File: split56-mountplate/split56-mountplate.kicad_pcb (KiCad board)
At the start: 2 copper layers, 139.2 x 82 mm, 12 parts

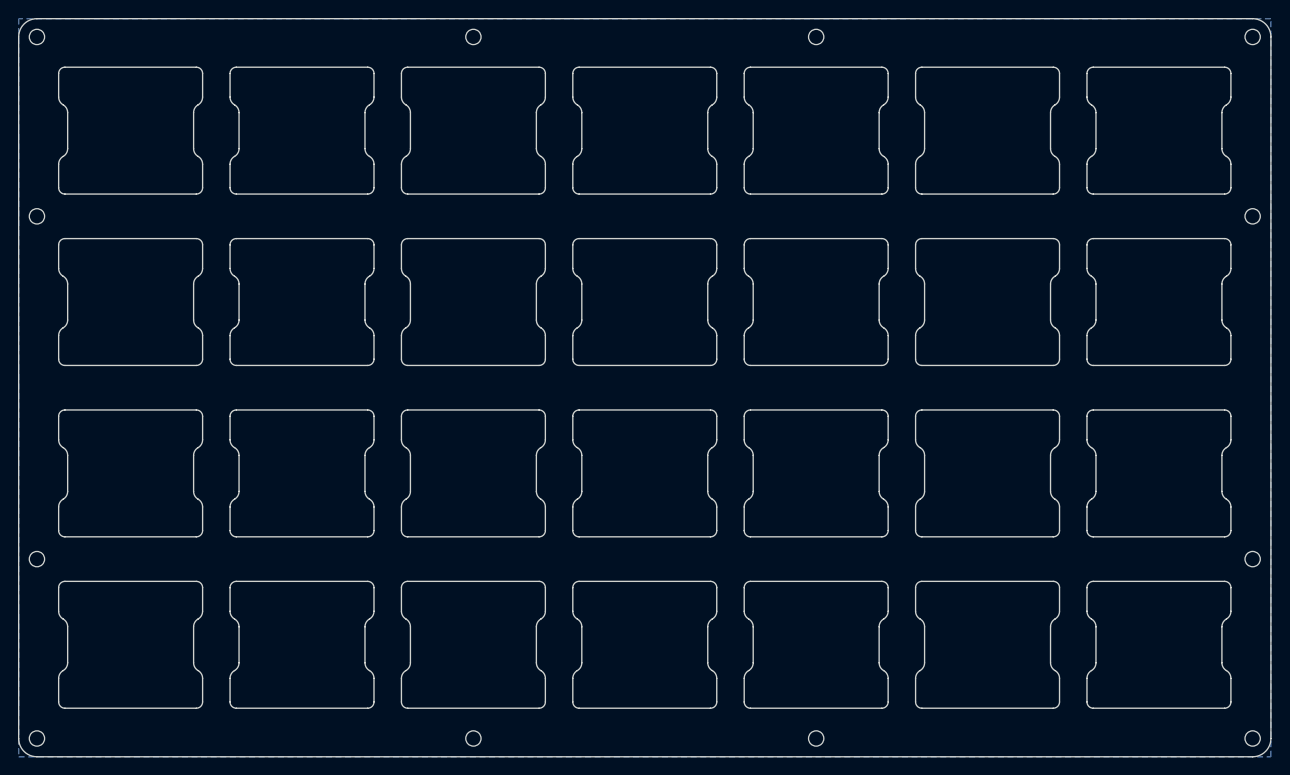
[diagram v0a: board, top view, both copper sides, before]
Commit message: Fix mount plate hole size
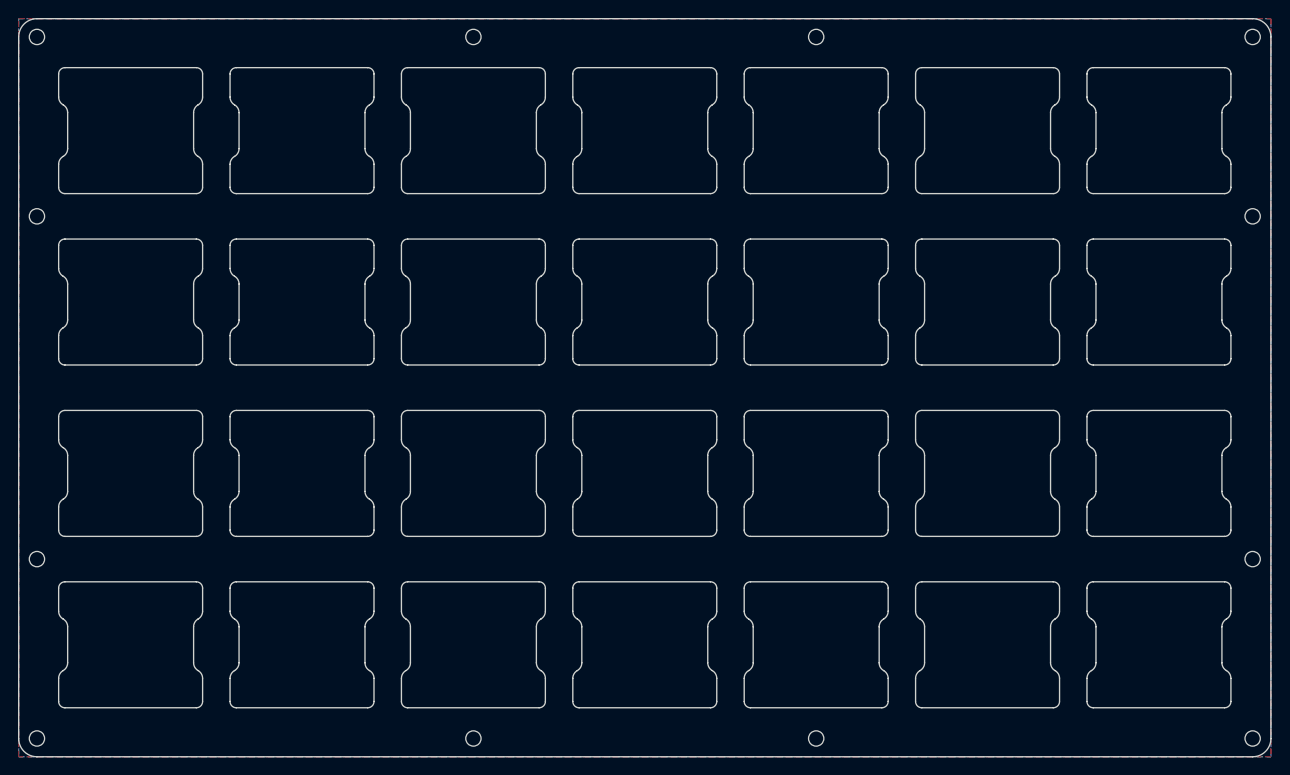
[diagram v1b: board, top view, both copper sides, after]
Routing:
- added copper zone on F.Cu, net (none)
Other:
- outline, holes or cut-outs redrawn
